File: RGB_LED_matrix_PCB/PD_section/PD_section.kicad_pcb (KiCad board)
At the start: 2 copper layers, 45 parts, among them Q1 AO4407A, Q2 AO4407A, Q3 AO3401A, U1 HUSB238A-xxxxx-QN16R, U2 TPS54202DDC

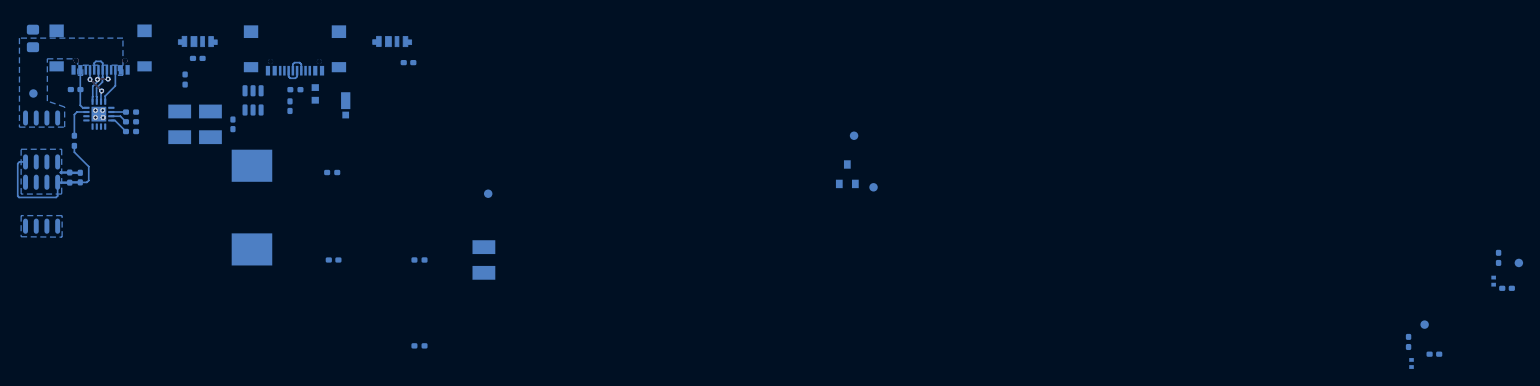
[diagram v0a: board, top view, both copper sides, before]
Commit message: Changed the USB connector to one that is compatible with higher PD voltages. Further proceeded with PD section routing
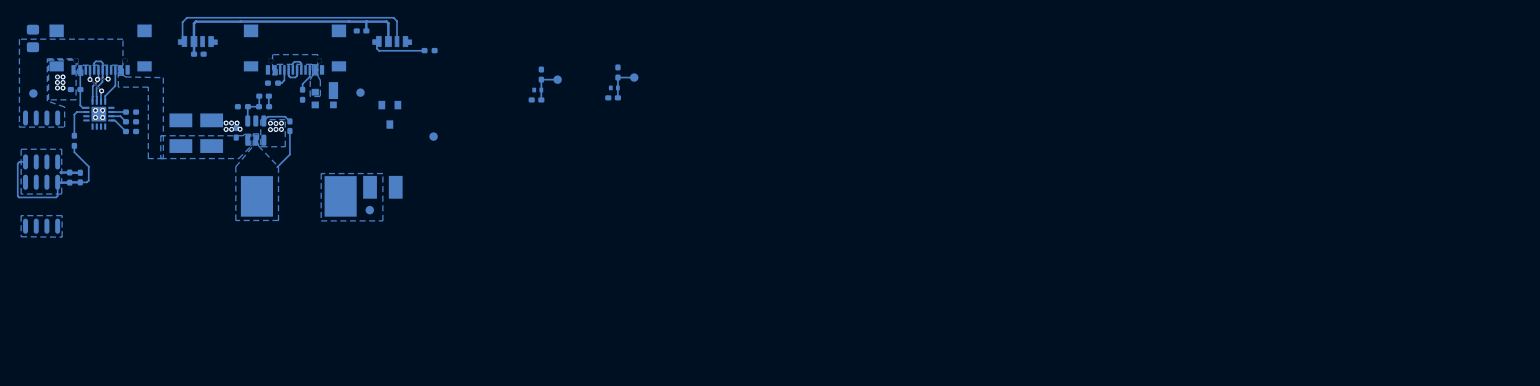
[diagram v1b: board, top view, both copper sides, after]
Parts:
- USB1, USB2: value TYPE-C 16P QTWT -> TYPE-C 16P QTGM027
- moved C9 117.0 mm to (138.6, 48.4)
- moved TP5 115.8 mm to (141.1, 46.0)
- moved D1 115.3 mm to (138.7, 47.2), turned to 0 degrees
- moved R9 115.3 mm to (139.2, 45.4)
- moved C10 101.8 mm to (147.6, 48.2)
- moved D2 99.8 mm to (147.8, 47.0), turned to 0 degrees
- moved R10 98.8 mm to (148.2, 45.2)
- moved TP6 98.0 mm to (150.1, 45.8)
- moved TP1 58.6 mm to (117.8, 47.5)
- moved Q3 54.6 mm to (121.2, 50.2), turned to 90 degrees
- moved TP3 52.4 mm to (126.4, 52.8)
- moved R8 35.2 mm to (103.8, 49.2)
- moved R11 29.1 mm to (125.9, 42.6), turned to 180 degrees
- moved R7 25.8 mm to (106.3, 49.2)
- moved C7 21.1 mm to (106.3, 48.0)
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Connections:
- C6 pad 2: Net-(Q3-D) -> Net-(Q3-S)
- C7 pad 1: Net-(Q3-D) -> Net-(Q3-S)
- L1 pad 2: Net-(Q3-D) -> Net-(Q3-S)
- LED1 pad 3: Net-(LED1-DOUT) -> /IND_LED_DOUT
- LED2 pad 1: Net-(LED1-DOUT) -> Net-(LED2-DIN)
- LED2 pad 3: /IND_LED_DOUT -> Net-(LED1-DIN)
- Q3 pad 2: +5V_VSYS -> Net-(Q3-S)
- Q3 pad 3: Net-(Q3-D) -> +5V_VSYS
- R11 pad 2: Net-(LED1-DIN) -> Net-(LED2-DIN)
- R7 pad 1: Net-(Q3-D) -> Net-(Q3-S)
- TP2 pad 1: Net-(Q3-D) -> Net-(Q3-S)
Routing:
- net Net-(LED1-DIN): track 0.00 -> 30.4 mm
- net +5V_VSYS: track 0.00 -> 30.1 mm
- net Net-(LED2-DIN): track 0.00 -> 6.60 mm
- net Net-(U2-SW): track 0.00 -> 4.90 mm
- net /CC2_read: track 0.00 -> 4.33 mm
- net /CC1_read: track 0.00 -> 4.33 mm
- net Net-(U2-FB): track 0.00 -> 4.22 mm
- net Net-(U2-BOOT): track 0.00 -> 3.53 mm
- net Net-(USB2-CC2): track 0.00 -> 2.69 mm
- net Net-(USB2-CC1): track 0.00 -> 2.13 mm
- net Net-(Q3-S): track 0.00 -> 1.26 mm
- net GND: vias 4 -> 22
- added copper zone on B.Cu, net GND
- added copper zone on B.Cu, net Net-(F1-Pad2)
- added copper zone on B.Cu, net Net-(Q3-S)
- added copper zone on B.Cu, net Net-(U2-SW)
